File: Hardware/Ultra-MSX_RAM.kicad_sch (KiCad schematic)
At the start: 5 parts, among them J13 Conn_SO-DIMM-74_MSX, U10 SST39SF040, U8 AS6C4008-55STIN

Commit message: Finished the VDP-board, finished up the mixer-section, removed the buffer-pins from the FPGA, and instead added external buffers for the slots, designed a marquee-block with the Ultra-MSX logo, designed the logotype, andmultiple other changes.
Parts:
- R80: footprint Resistor_SMD:R_0603_1608Metric_Pad0.98x0.95mm_HandSolder -> LRJ:R_0603_1608Metric_roundcourt
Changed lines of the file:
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@@
   (title_block
     (title "ULTRA-MSX")
+    (date "2022-06-05")
     (rev "A-A")
   )
@@
       (effects (font (size 1.27 1.27)) (justify left) hide)
     )
-    (property "Footprint" "Resistor_SMD:R_0603_1608Metric_Pad0.98x0.95mm_HandSolder" (id 2) (at 30.48 49.53 0)
+    (property "Footprint" "LRJ:R_0603_1608Metric_roundcourt" (id 2) (at 30.48 49.53 0)
       (effects (font (size 1.27 1.27)) hide)
     )

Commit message: Added SD-card slot, made basic 3d-model for sd-card slot, connected it up in the schematic, and numerous other tweaks.
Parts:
- added C10: C_GRM21BR61A476ME15K, Capacitor_SMD:C_0805_2012Metric, symbol LRJ-parts:C_GRM21BR61A476ME15K
- added J10: Micro_SD_Card_Det_GCT, LRJ:microSD_HC_GCT_MEM2061, symbol LRJ-parts:Micro_SD_Card_Det_GCT
- added R36: R_ERJ-3GEYJ105V, Resistor_SMD:R_0603_1608Metric, symbol LRJ-parts:R_ERJ-3GEYJ105V
- added R37, R38: R_RC0603FR-074K7L, Resistor_SMD:R_0603_1608Metric, symbol LRJ-parts:R_RC0603FR-074K7L
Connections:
- net GND: now also C10.1, R36.2
- new net: J10.6 (VSS), R36.1
- new net +3V3: J10.4 (VDD), R37.2, R38.2
- new net SDSH: C10.2, J10.11 (SHIELD)
- new net SD_CLK: J10.5 (CLK)
- new net SD_CMD: J10.3 (CMD)
- new net SD_DAT1: J10.8 (DAT1)
- new net SD_DAT3: J10.2 (DAT3/CD)
- new net SD_DET_A: J10.10 (DET_A), R38.1
- new net SD_DET_B: J10.9 (DET_B), R37.1
- new net SD_MISO/DAT0: J10.7 (DAT0)
- new net SD_MOSI/DAT2: J10.1 (DAT2)
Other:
- note added: "MSX2SD https://github.com/fbelavenuto/msxsdmapperv2"
- note removed: "Data"

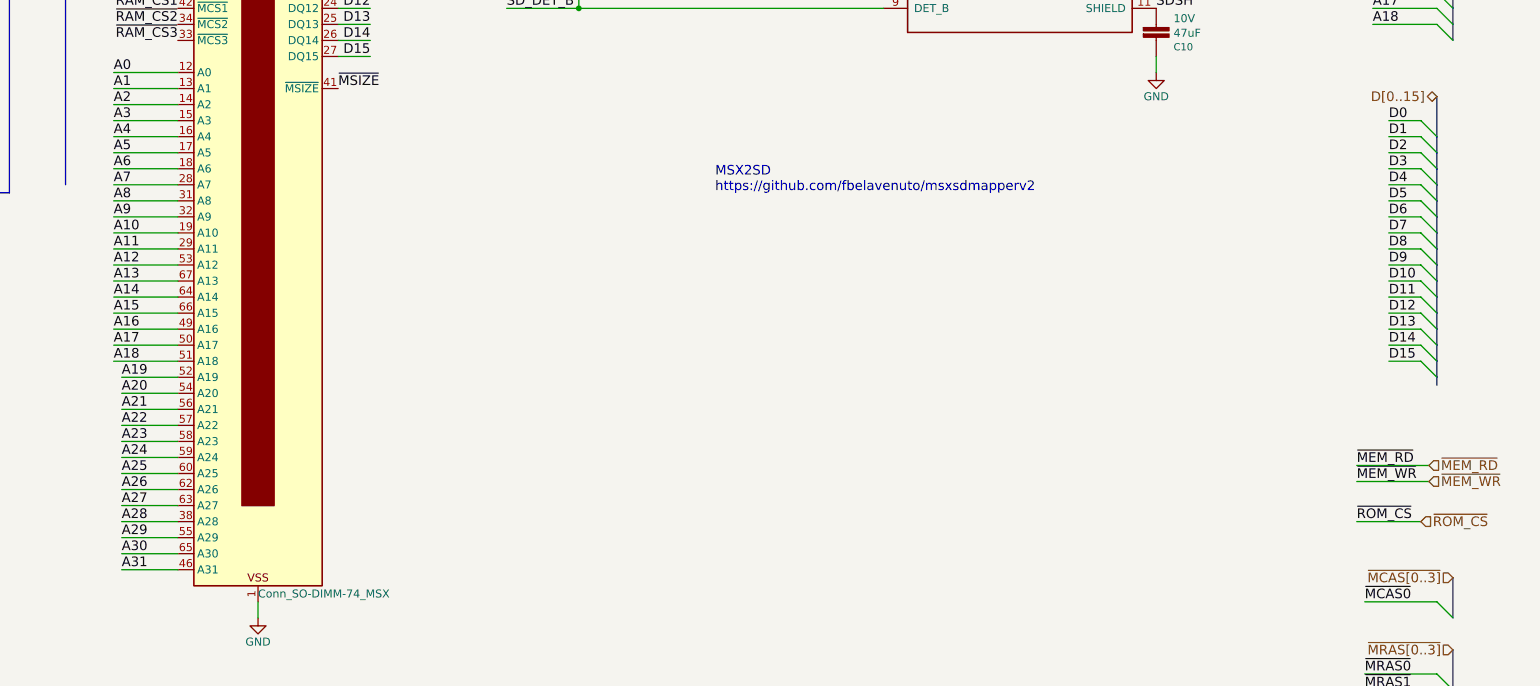
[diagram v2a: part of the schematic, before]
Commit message: Redesigned VDP-board to include a socket, increased it to 4 layers. Various clean-ups here and there. Improved the printer-port and joystick-port 3D-models. Improved the cooling-fin 3D-model, and added attachment-spring in 3D-model.
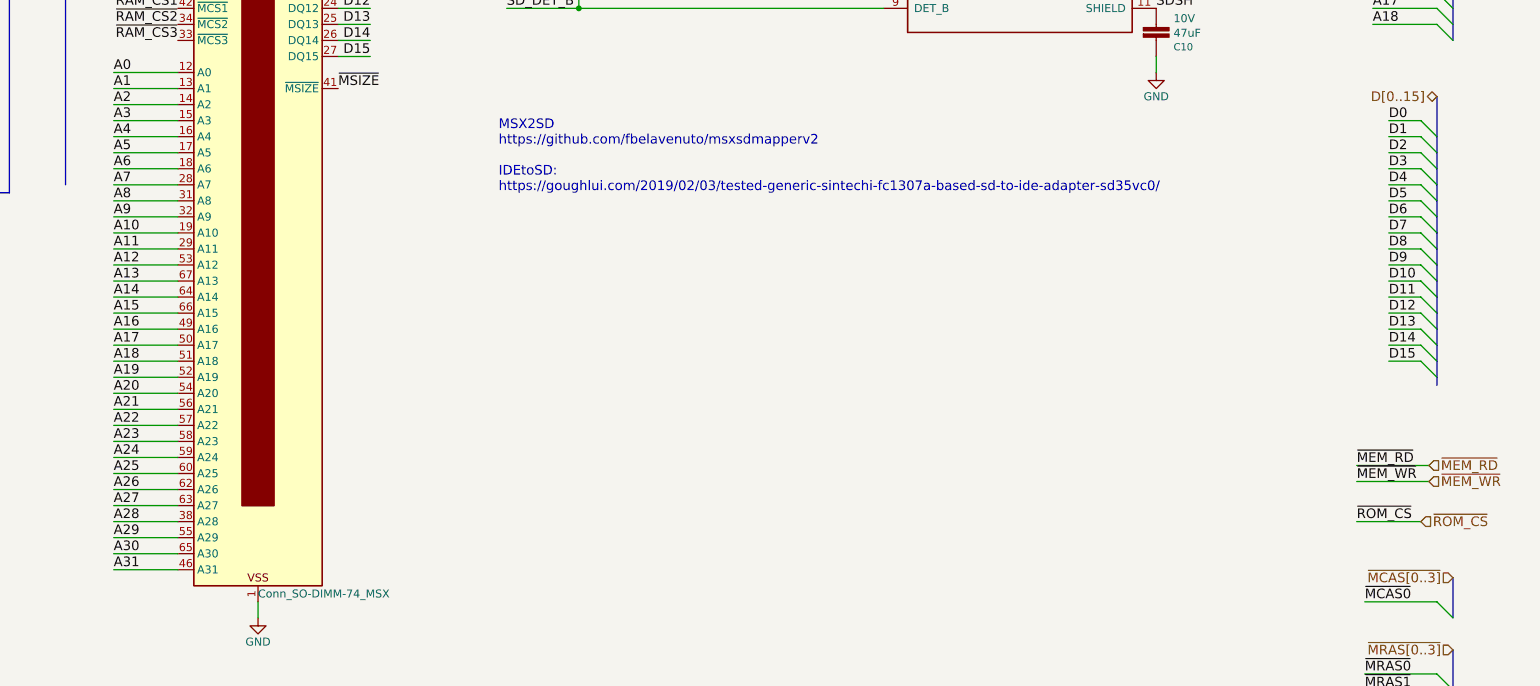
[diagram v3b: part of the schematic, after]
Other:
- note added: "MSX2SD https://github.com/fbelavenuto/msxsdmapperv2 IDEtoSD: https://goughlui.com/2019/02/03/tested-generic-sintechi-fc1307a-based-sd-to-ide-adapter-sd35vc0/"
- note removed: "MSX2SD https://github.com/fbelavenuto/msxsdmapperv2"
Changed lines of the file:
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@@
     (stroke (width 0) (type default) (color 0 0 0 0))
   )
-  (wire (pts (xy 196.85 128.27) (xy 187.96 128.27))
+  (wire (pts (xy 186.69 128.27) (xy 196.85 128.27))
     (stroke (width 0) (type default) (color 0 0 0 0))
   )
@@
     (stroke (width 0) (type default) (color 0 0 0 0))
   )
-  (wire (pts (xy 196.85 148.59) (xy 187.96 148.59))
+  (wire (pts (xy 186.69 148.59) (xy 196.85 148.59))
     (stroke (width 0) (type default) (color 0 0 0 0))
   )
@@
     (stroke (width 0) (type default) (color 0 0 0 0))
   )
-  (wire (pts (xy 196.85 130.81) (xy 187.96 130.81))
+  (wire (pts (xy 186.69 130.81) (xy 196.85 130.81))
     (stroke (width 0) (type default) (color 0 0 0 0))
   )
@@
     (stroke (width 0) (type default) (color 0 0 0 0))
   )
-  (wire (pts (xy 196.85 143.51) (xy 187.96 143.51))
+  (wire (pts (xy 186.69 143.51) (xy 196.85 143.51))
     (stroke (width 0) (type default) (color 0 0 0 0))
   )
@@
     (stroke (width 0) (type default) (color 0 0 0 0))
   )
+  (wire (pts (xy 186.69 133.35) (xy 196.85 133.35))
+    (stroke (width 0) (type default) (color 0 0 0 0))
+  )
   (bus (pts (xy 398.78 59.69) (xy 398.78 62.23))
     (stroke (width 0) (type default) (color 0 0 0 0))
@@
     (stroke (width 0) (type default) (color 0 0 0 0))
   )
-  (wire (pts (xy 196.85 151.13) (xy 187.96 151.13))
-    (stroke (width 0) (type default) (color 0 0 0 0))
-  )
-  (wire (pts (xy 196.85 138.43) (xy 187.96 138.43))
+  (wire (pts (xy 186.69 138.43) (xy 196.85 138.43))
     (stroke (width 0) (type default) (color 0 0 0 0))
   )
@@
     (stroke (width 0) (type default) (color 0 0 0 0))
   )
+  (wire (pts (xy 186.69 153.67) (xy 196.85 153.67))
+    (stroke (width 0) (type default) (color 0 0 0 0))
+  )
   (wire (pts (xy 26.67 88.9) (xy 26.67 91.44))
     (stroke (width 0) (type default) (color 0 0 0 0))
@@
     (stroke (width 0) (type default) (color 0 0 0 0))
   )
-  (wire (pts (xy 196.85 146.05) (xy 187.96 146.05))
+  (wire (pts (xy 186.69 146.05) (xy 196.85 146.05))
     (stroke (width 0) (type default) (color 0 0 0 0))
   )
@@
     (stroke (width 0) (type default) (color 0 0 0 0))
   )
-  (wire (pts (xy 196.85 133.35) (xy 187.96 133.35))
-    (stroke (width 0) (type default) (color 0 0 0 0))
-  )
-  (wire (pts (xy 196.85 156.21) (xy 187.96 156.21))
+  (wire (pts (xy 186.69 156.21) (xy 196.85 156.21))
     (stroke (width 0) (type default) (color 0 0 0 0))
   )
@@
     (stroke (width 0) (type default) (color 0 0 0 0))
   )
-  (wire (pts (xy 196.85 153.67) (xy 187.96 153.67))
-    (stroke (width 0) (type default) (color 0 0 0 0))
-  )
   (wire (pts (xy 196.85 87.63) (xy 186.69 87.63))
     (stroke (width 0) (type default) (color 0 0 0 0))
@@
     (stroke (width 0) (type default) (color 0 0 0 0))
   )
-  (wire (pts (xy 196.85 135.89) (xy 187.96 135.89))
+  (wire (pts (xy 186.69 135.89) (xy 196.85 135.89))
     (stroke (width 0) (type default) (color 0 0 0 0))
   )
@@
     (stroke (width 0) (type default) (color 0 0 0 0))
   )
+  (wire (pts (xy 186.69 151.13) (xy 196.85 151.13))
+    (stroke (width 0) (type default) (color 0 0 0 0))
+  )
   (wire (pts (xy 129.54 60.96) (xy 119.38 60.96))
     (stroke (width 0) (type default) (color 0 0 0 0))
@@
     (stroke (width 0) (type default) (color 0 0 0 0))
   )
-  (wire (pts (xy 196.85 158.75) (xy 187.96 158.75))
-    (stroke (width 0) (type default) (color 0 0 0 0))
-  )
   (wire (pts (xy 149.86 40.64) (xy 158.75 40.64))
     (stroke (width 0) (type default) (color 0 0 0 0))
@@
     (stroke (width 0) (type default) (color 0 0 0 0))
   )
+  (wire (pts (xy 186.69 158.75) (xy 196.85 158.75))
+    (stroke (width 0) (type default) (color 0 0 0 0))
+  )
   (wire (pts (xy 129.54 48.26) (xy 119.38 48.26))
     (stroke (width 0) (type default) (color 0 0 0 0))
@@
     (stroke (width 0) (type default) (color 0 0 0 0))
   )
-  (wire (pts (xy 196.85 140.97) (xy 187.96 140.97))
+  (wire (pts (xy 186.69 140.97) (xy 196.85 140.97))
     (stroke (width 0) (type default) (color 0 0 0 0))
   )
@@
     (effects (font (size 1.524 1.524)) (justify left bottom))
   )
-  (text "MSX2SD\nhttps://github.com/fbelavenuto/msxsdmapperv2"
-    (at 281.94 99.06 0)
+  (text "MSX2SD\nhttps://github.com/fbelavenuto/msxsdmapperv2\n\nIDEtoSD:\nhttps://goughlui.com/2019/02/03/tested-generic-sintechi-fc1307a-based-sd-to-ide-adapter-sd35vc0/"
+    (at 247.65 99.06 0)
     (effects (font (size 1.524 1.524)) (justify left bottom))
   )
@@
     (effects (font (size 1.524 1.524)) (justify left bottom))
   )
-  (label "A27" (at 187.96 148.59 0)
+  (label "A27" (at 186.69 148.59 0)
     (effects (font (size 1.524 1.524)) (justify left bottom))
   )
@@
     (effects (font (size 1.524 1.524)) (justify left bottom))
   )
-  (label "A23" (at 187.96 138.43 0)
+  (label "A23" (at 186.69 138.43 0)
     (effects (font (size 1.524 1.524)) (justify left bottom))
   )
@@
     (effects (font (size 1.524 1.524)) (justify left bottom))
   )
-  (label "A19" (at 187.96 128.27 0)
+  (label "A19" (at 186.69 128.27 0)
     (effects (font (size 1.524 1.524)) (justify left bottom))
   )
@@
     (effects (font (size 1.524 1.524)) (justify left bottom))
   )
-  (label "A31" (at 187.96 158.75 0)
+  (label "A31" (at 186.69 158.75 0)
     (effects (font (size 1.524 1.524)) (justify left bottom))
   )
@@
     (effects (font (size 1.524 1.524)) (justify left bottom))
   )
-  (label "A26" (at 187.96 146.05 0)
+  (label "A26" (at 186.69 146.05 0)
     (effects (font (size 1.524 1.524)) (justify left bottom))
   )
@@
     (effects (font (size 1.524 1.524)) (justify left bottom))
   )
-  (label "A21" (at 187.96 133.35 0)
+  (label "A21" (at 186.69 133.35 0)
     (effects (font (size 1.524 1.524)) (justify left bottom))
   )
@@
     (effects (font (size 1.524 1.524)) (justify right bottom))
   )
-  (label "A25" (at 187.96 143.51 0)
+  (label "A25" (at 186.69 143.51 0)
     (effects (font (size 1.524 1.524)) (justify left bottom))
   )
@@
     (effects (font (size 1.524 1.524)) (justify left bottom))
   )
-  (label "A20" (at 187.96 130.81 0)
-    (effects (font (size 1.524 1.524)) (justify left bottom))
-  )
-  (label "A24" (at 187.96 140.97 0)
+  (label "A20" (at 186.69 130.81 0)
+    (effects (font (size 1.524 1.524)) (justify left bottom))
+  )
+  (label "A24" (at 186.69 140.97 0)
     (effects (font (size 1.524 1.524)) (justify left bottom))
   )
@@
     (effects (font (size 1.524 1.524)) (justify left bottom))
   )
-  (label "A22" (at 187.96 135.89 0)
+  (label "A22" (at 186.69 135.89 0)
     (effects (font (size 1.524 1.524)) (justify left bottom))
   )
@@
     (effects (font (size 1.524 1.524)) (justify left bottom))
   )
-  (label "A28" (at 187.96 151.13 0)
-    (effects (font (size 1.524 1.524)) (justify left bottom))
-  )
-  (label "A30" (at 187.96 156.21 0)
+  (label "A28" (at 186.69 151.13 0)
+    (effects (font (size 1.524 1.524)) (justify left bottom))
+  )
+  (label "A30" (at 186.69 156.21 0)
     (effects (font (size 1.524 1.524)) (justify left bottom))
   )
@@
     (effects (font (size 1.524 1.524)) (justify left bottom))
   )
-  (label "A29" (at 187.96 153.67 0)
-    (effects (font (size 1.524 1.524)) (justify left bottom))
-  )
+  (label "A29" (at 186.69 153.67 0)
+    (effects (font (size 1.524 1.524)) (justify left bottom))
+  )

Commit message: Generated first PDF-files
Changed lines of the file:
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@@
   )
   (text "Z80380 Evaluation Board\n---------------------\n+CMOS 80380 MPU\n*18.432 MHz Oscillator\n+1 Socketed 48KB EPROM\n\n1 Socketed 128KB (128x8) SRAM\n\n2 Unsocketed 128KB (1 Mb) DRAM Slots\n\nReset Switch\nNMI Switch"
-    (at 425.45 146.05 0)
+    (at 245.11 235.585 0)
     (effects (font (size 1.524 1.524)) (justify left bottom))
   )
@@
   )
   (text "Look into an address-decoder for interfacing \nsmaller address-bus memory chips with the CPU.\n\nPriority Encoder is the name of one such.\n\nNote:\nThe i80386SX uses 72-pin sims for memory-modules.\n\nAn example of an encoder/controller for a 386DX:\nhttp://www.s100computers.com/My%20System%20Pages/80386%20Board/80386%20CPU%20Board.htm\n\n\nRam-chip suggestion:\nCY62167ELL-45ZXIT (2 MB, 20 Address, 16 Data)\n\nIS42S16320D-7BLI (512 MB, 14 Address, 16 Data)\n\n"
-    (at 426.72 77.47 0)
+    (at 245.745 199.39 0)
     (effects (font (size 1.524 1.524)) (justify left bottom))
   )
@@
   )
   (text "Memory-slot suggestions:\nG42V12352HR\nHSEC8-137-01-L-DV-A"
-    (at 425.45 158.75 0)
+    (at 245.11 245.745 0)
     (effects (font (size 1.524 1.524)) (justify left bottom))
   )
   (text "Talk to Jurjen Kranenborg \nabout the Z380 and system\ndesign:\n------------------\nhttps://www.kranenborg.org/"
-    (at 424.18 101.6 0)
+    (at 20.32 249.555 0)
     (effects (font (size 1.524 1.524)) (justify left bottom))
   )
@@
   )
   (text "My own memory-module:\n32 Address\n16 Data\nMHEN\nLHEN\nCS1\nCS2\nCS3\nCS4\nMEMRD\nMEMWR\n\n56 pins\n\n\nSO-DIMM-144-modules:\n64+4+8 = 76 I/O"
-    (at 426.72 30.48 0)
+    (at 245.745 152.4 0)
     (effects (font (size 1.524 1.524)) (justify left bottom))
   )

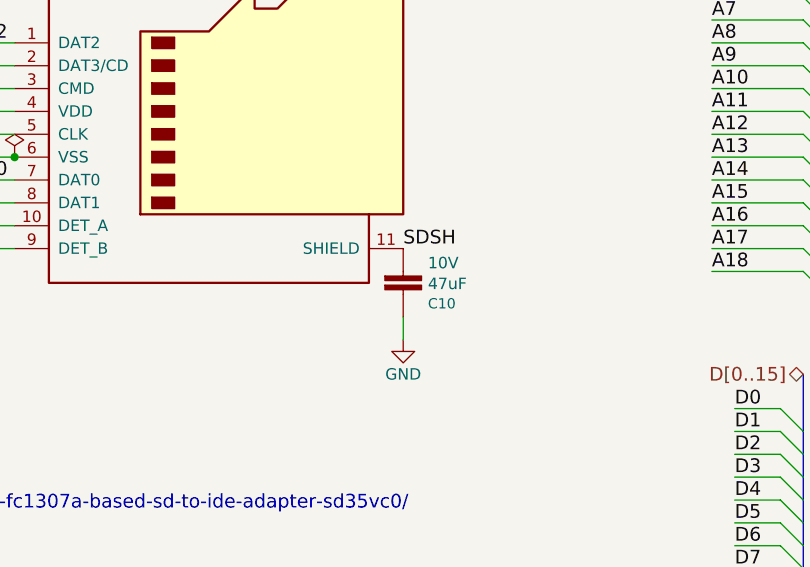
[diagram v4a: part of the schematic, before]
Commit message: Multiple redesigns of the IO-shield. Replaced FPGA with lower pin-count AT10K, since the higher pin-count one is now obsolete.
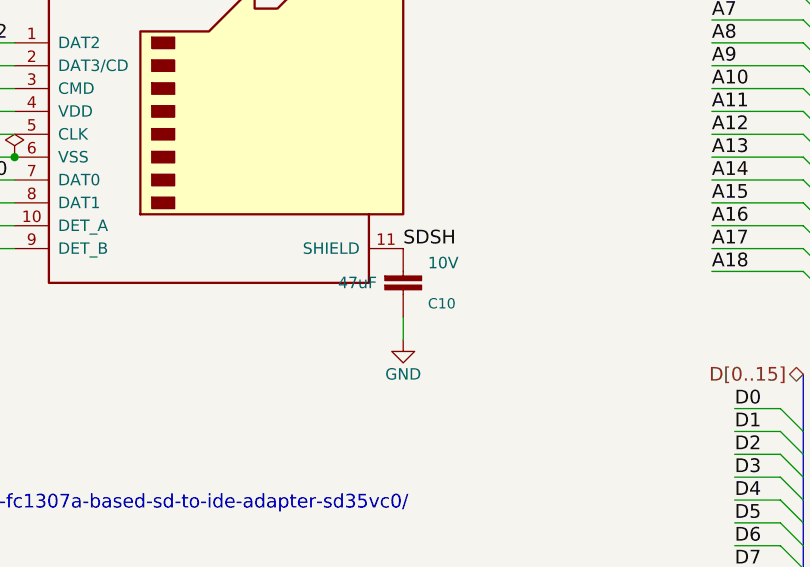
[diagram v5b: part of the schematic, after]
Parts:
- C10: Capacitance (none) -> 47uF; Capacity 47uF -> (none)
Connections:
- net +3V3 renamed +3.3V
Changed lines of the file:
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@@
       (effects (font (size 1.27 1.27)) hide)
-    )
-    (property "Capacity" "47uF" (id 4) (at 354.5332 73.7616 0)
-      (effects (font (size 1.27 1.27)) (justify left))
     )
     (property "Manufacturer" "Murata Electronics " (id 5) (at 367.03 80.01 0)
@@
       (effects (font (size 1.524 1.524)) hide)
     )
+    (property "Capacitance" "47uF" (id 10) (at 346.71 73.66 0))
     (pin "1")
     (pin "2")

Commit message: Added cooler and CPU-mount footprints, as well as Indication LEDs.
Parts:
- removed J13: Conn_SO-DIMM-74_MSX, LRJ:SAMTEC_HSEC8-137-01-X-DV-A, symbol Ultra-MSX:Conn_SO-DIMM-74_MSX
- removed U8: AS6C4008-55STIN, Ultra-MSX:sTSOP-32_13.4x8mm_P0.5mm, symbol LRJ-parts:AS6C4008-55STIN
- added J13: TE_Conn_5822019-4, LRJ:SIMM-72_socket, symbol LRJ-parts:TE_Conn_5822019-4
- added R55: R_ERJ-3GEYJ105V, Resistor_SMD:R_0603_1608Metric, symbol LRJ-parts:R_ERJ-3GEYJ105V
- added U8: AS6C8008-55ZIN, Package_SO:TSOP-II-44_10.16x18.41mm_P0.8mm, symbol LRJ-parts:AS6C8008-55ZIN
- J10: Current rating (none) -> 0.5A; Voltage rating (none) -> 63V
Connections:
- net +3.3V: now also C10.2
- net +5V: now also J13.10 (VCC), J13.30 (VCC), J13.59 (VCC)
- net A0: now also U8.5 (A0)
- net A1: now also U8.4 (A1)
- net A10: now also U8.27 (A10)
- net A11: now also U8.26 (A11)
- net A12: now also U8.25 (A12)
- net A13: now also U8.24 (A13)
- net A14: now also U8.23 (A14)
- net A15: now also U8.22 (A15)
- net A16: now also U8.21 (A16)
- net A17: now also U8.20 (A17)
- net A18: now also U8.19 (A18)
- net A19: now also J13.12 (A0), U8.18 (A19)
- net A2: now also U8.3 (A2)
- net A20: now also J13.13 (A1)
- net A21: now also J13.14 (A2)
- net A22: now also J13.15 (A3)
- net A23: now also J13.16 (A4)
- net A24: now also J13.17 (A5)
- net A25: now also J13.18 (A6)
- net A26: now also J13.28 (A7)
- net A27: now also J13.31 (A8)
- net A28: now also J13.32 (A9)
- net A29: now also J13.19 (A10)
- net A3: now also U8.2 (A3)
- net A30: now also J13.29 (A11)
- net A4: now also U8.1 (A4)
- net A5: now also U8.44 (A5)
- net A6: now also U8.43 (A6)
- net A7: now also U8.42 (A7)
- net A8: now also U8.39 (A8)
- net A9: now also U8.28 (A9)
- net D0: now also U8.9 (DQ0)
- net D1: now also U8.10 (DQ1)
- net D2: now also U8.13 (DQ2)
- net D3: now also U8.14 (DQ3)
- net D4: now also U8.31 (DQ4)
- net D5: now also U8.32 (DQ5)
- net D6: now also U8.35 (DQ6)
- net D7: now also U8.36 (DQ7)
- net GND: now also J10.6 (VSS), J13.1 (VSS), J13.39 (VSS), J13.72 (VSS), R55.1
- net ~{MEM_RD}: now also U8.41 (~{OE})
- net ~{MEM_WR}: now also U8.17 (~{WE})
- net ~{RAM_CS0}: now also U8.6 (~{CE})
- net ~{UMCS}: now also J13.47 (~{WE})
- net at R36.1: no longer J10.6 (VSS)
- net SDSH: no longer names the net of J10.11 (SHIELD)
- net SDSH: now also R55.2; no longer C10.2
- new net MD0: J13.2 (DQ0)
- new net MD1: J13.4 (DQ1)
- new net MD10: J13.53 (DQ10)
- new net MD11: J13.55 (DQ11)
- new net MD12: J13.57 (DQ12)
- new net MD13: J13.61 (DQ13)
- new net MD14: J13.63 (DQ14)
- new net MD15: J13.65 (DQ15)
- new net MD16: J13.3 (DQ16)
- new net MD17: J13.5 (DQ17)
- new net MD18: J13.7 (DQ18)
- new net MD19: J13.9 (DQ19)
- new net MD2: J13.6 (DQ2)
- new net MD20: J13.21 (DQ20)
- new net MD21: J13.23 (DQ21)
- new net MD22: J13.25 (DQ22)
- new net MD23: J13.27 (DQ23)
- new net MD24: J13.50 (DQ24)
- new net MD25: J13.52 (DQ25)
- new net MD26: J13.54 (DQ26)
- new net MD27: J13.56 (DQ27)
- new net MD28: J13.58 (DQ28)
- new net MD29: J13.60 (DQ29)
- new net MD3: J13.8 (DQ3)
- new net MD30: J13.62 (DQ30)
- new net MD31: J13.64 (DQ31)
- new net MD4: J13.20 (DQ4)
- new net MD5: J13.22 (DQ5)
- new net MD6: J13.24 (DQ6)
- new net MD7: J13.26 (DQ7)
- new net MD8: J13.49 (DQ8)
- new net MD9: J13.51 (DQ9)
- new net MP1: J13.67 (PD1)
- new net MP2: J13.68 (PD2)
- new net MP3: J13.69 (PD3)
- new net MP4: J13.70 (PD4)
- new net ~{CAS0}: J13.40 (~{CAS0})
- new net ~{RAS0}: J13.44 (~{RAS0})
- new net ~{RAS1}: J13.45 (~{RAS1})
- no-connect marks 1 -> 0
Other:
- note added: "Less common ram-sizes for SIMM-72 EDO ram include 128MB."
- note added: "Open source memory controllers: --------------------------- https://web.archive.org/web/20191020220315/http://hamsterworks.co.nz/mediawiki/index.php/SDRAM_Memory_Controller https://web.archive.org/web/20191020145937/http://hamsterworks.co.nz/mediawiki/index.php/Simple_SDRAM_Controller https://github.com/alvieboy/ZPUino-HDL/blob/dcache/zpu/hdl/zpuino/boards/papilio-pro/S6LX9/sdram_hamster.vhd http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"
- note added: "RAM module"
- note added: "Suggestion for memory controller, instead of FPGA: MKE14F512VLL16 (mcu)"
- note removed: "SDRAM module"
- moved on the sheet: C10, R36
